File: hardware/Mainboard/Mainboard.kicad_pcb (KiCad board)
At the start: 2 copper layers, 9 parts, among them CN1 NUCLE_F446RE_MORPHO_CN7, CN2 NUCLE_F446RE_MORPHO_CN10, Q2 PSMN5R2-60YL, Q4 PSMN5R2-60YL, Q5 PSMN5R2-60YL, Q6 PSMN5R2-60YL, Q7 AO3400A, Q8 AO3400A, U10 TMC2209_SILENTSTEPSTICK

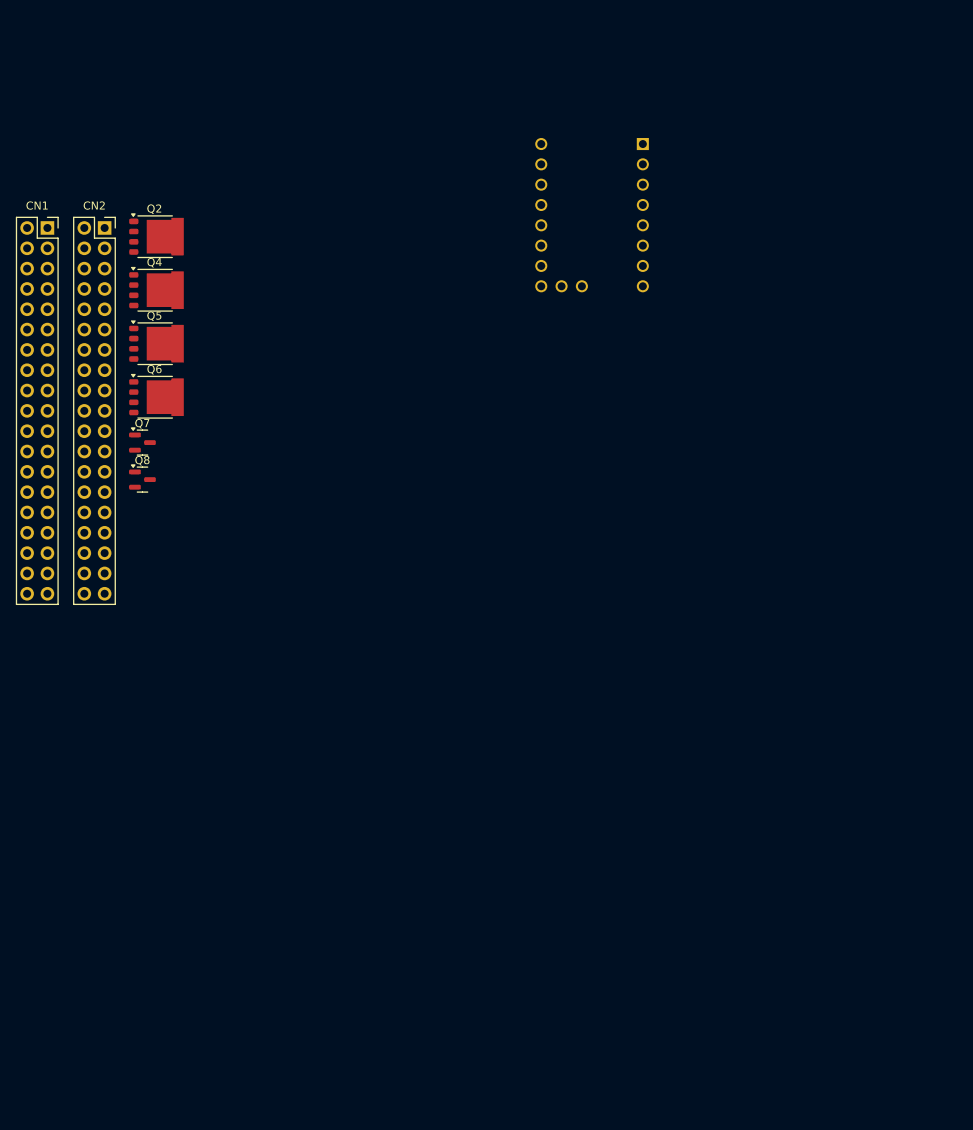
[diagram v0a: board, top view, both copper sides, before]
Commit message: Mainboard-3
Version 3 of Mainboard, (version 2 not uploaded)
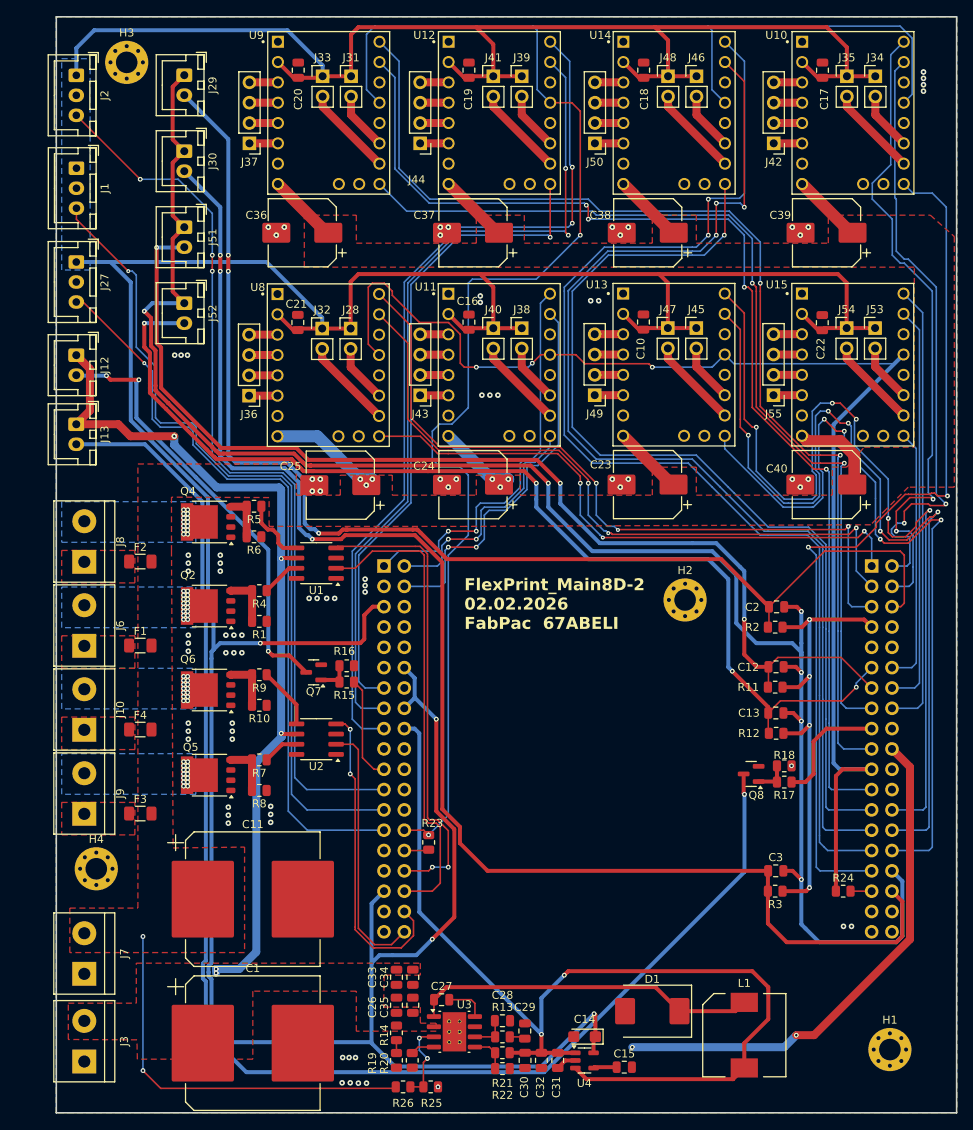
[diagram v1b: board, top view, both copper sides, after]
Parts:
- added C1: 470µ, Capacitor_SMD:CP_Elec_16x17.5, F.Cu at (98.6, 151.0)
- added C10: 100n, Capacitor_SMD:C_0805_2012Metric, F.Cu at (147.4, 60.9)
- added C11: 470µ, Capacitor_SMD:CP_Elec_16x17.5, F.Cu at (98.6, 133.0)
- added C12: 10u, Capacitor_SMD:C_0805_2012Metric, F.Cu at (164.0, 104.0)
- added C13: 10u, Capacitor_SMD:C_0805_2012Metric, F.Cu at (163.9, 109.7)
- added C14: 2.2uF (tantal), Capacitor_Tantalum_SMD:CP_EIA-3216-10_Kemet-I, F.Cu at (140.0, 150.2)
- added C15: 470pF, Capacitor_SMD:C_0805_2012Metric, F.Cu at (145.0, 154.0)
- added C16: 100n, Capacitor_SMD:C_0805_2012Metric, F.Cu at (125.6, 60.9)
- added C17: 100n, Capacitor_SMD:C_0805_2012Metric, F.Cu at (169.8, 29.4)
- added C18: 100n, Capacitor_SMD:C_0805_2012Metric, F.Cu at (147.4, 29.4)
- added C19: 100n, Capacitor_SMD:C_0805_2012Metric, F.Cu at (125.6, 29.4)
- added C2: 10u, Capacitor_SMD:C_0805_2012Metric, F.Cu at (164.0, 96.5)
- added C20: 100n, Capacitor_SMD:C_0805_2012Metric, F.Cu at (104.2, 29.4)
- added C21: 100n, Capacitor_SMD:C_0805_2012Metric, F.Cu at (104.2, 60.9)
- added C22: 100n, Capacitor_SMD:C_0805_2012Metric, F.Cu at (169.7, 60.9)
- added C23: 100µ, Capacitor_SMD:CP_Elec_8x10, F.Cu at (147.9, 81.2)
- added C24: 100µ, Capacitor_SMD:CP_Elec_8x10, F.Cu at (126.1, 81.2)
- added C25: 100µ, Capacitor_SMD:CP_Elec_8x10, F.Cu at (109.5, 81.2)
- added C26: 2.2uF, Capacitor_SMD:C_0805_2012Metric, F.Cu at (116.5, 146.3)
- added C27: 0.1uF, Capacitor_SMD:C_0805_2012Metric, F.Cu at (122.2, 145.6)
- added C28: 4.7pF, Capacitor_SMD:C_0805_2012Metric, F.Cu at (129.8, 148.2)
- added C29: 4.7nF, Capacitor_SMD:C_0805_2012Metric, F.Cu at (132.6, 149.5)
- added C3: 10u, Capacitor_SMD:C_0805_2012Metric, F.Cu at (163.9, 129.5)
- added C30: 47uF, Capacitor_SMD:C_0805_2012Metric, F.Cu at (132.6, 153.1)
- added C31: 47uF, Capacitor_SMD:C_0805_2012Metric, F.Cu at (136.7, 153.2)
- added C32: 47uF, Capacitor_SMD:C_0805_2012Metric, F.Cu at (134.6, 153.2)
- added C33: 2.2uF, Capacitor_SMD:C_0805_2012Metric, F.Cu at (116.5, 142.8)
- added C34: 2.2uF, Capacitor_SMD:C_0805_2012Metric, F.Cu at (118.6, 142.8)
- added C35: 2.2uF, Capacitor_SMD:C_0805_2012Metric, F.Cu at (118.6, 146.3)
- added C36: 100µ, Capacitor_SMD:CP_Elec_8x10, F.Cu at (104.8, 49.7)
- added C37: 100µ, Capacitor_SMD:CP_Elec_8x10, F.Cu at (126.1, 49.7)
- added C38: 100µ, Capacitor_SMD:CP_Elec_8x10, F.Cu at (147.9, 49.7)
- added C39: 100µ, Capacitor_SMD:CP_Elec_8x10, F.Cu at (170.3, 49.7)
- added C40: 100µ, Capacitor_SMD:CP_Elec_8x10, F.Cu at (170.3, 81.2)
- added D1: B560C, Diode_SMD:D_SMC, F.Cu at (148.5, 147.0)
- added F1: 3A, Fuse:Fuse_1206_3216Metric, F.Cu at (84.5, 101.3)
- added F2: 3A, Fuse:Fuse_1206_3216Metric, F.Cu at (84.5, 90.8)
- added F3: 15A, Fuse:Fuse_1206_3216Metric, F.Cu at (84.5, 122.3)
- added F4: Fuse, Fuse:Fuse_1206_3216Metric, F.Cu at (84.5, 111.8)
- added H1: MountingHole, MountingHole:MountingHole_2.7mm_M2.5_Pad_Via, F.Cu at (178.2, 151.8)
- added H2: MountingHole, MountingHole:MountingHole_2.7mm_M2.5_Pad_Via, F.Cu at (152.6, 95.6)
- added H3: MountingHole, MountingHole:MountingHole_2.7mm_M2.5_Pad_Via, F.Cu at (82.8, 28.4)
- added H4: MountingHole, MountingHole:MountingHole_2.7mm_M2.5_Pad_Via, F.Cu at (79.0, 129.2)
- added J1: X_END, Connector_JST:JST_XH_B3B-XH-A_1x03_P2.50mm_Vertical, F.Cu at (76.5, 41.6)
- added J10: Power, TerminalBlock:TerminalBlock_bornier-2_P5.08mm, F.Cu at (77.5, 111.8)
- added J12: Part_Cooling2, Connector_JST:JST_XH_B2B-XH-A_1x02_P2.50mm_Vertical, F.Cu at (76.5, 65.0)
- added J13: Part_Cooling1, Connector_JST:JST_XH_B2B-XH-A_1x02_P2.50mm_Vertical, F.Cu at (76.5, 73.6)
- added J2: Y_END, Connector_JST:JST_XH_B3B-XH-A_1x03_P2.50mm_Vertical, F.Cu at (76.5, 30.0)
- added J27: Z_END, Connector_JST:JST_XH_B3B-XH-A_1x03_P2.50mm_Vertical, F.Cu at (76.5, 53.4)
- added J28: X_MS2, Connector_PinHeader_2.54mm:PinHeader_1x02_P2.54mm_Vertical, F.Cu at (110.8, 61.7)
- added J29: HE1_therm, Connector_JST:JST_XH_B2B-XH-A_1x02_P2.50mm_Vertical, F.Cu at (90.0, 30.0)
- added J3: +12V, TerminalBlock:TerminalBlock_bornier-2_P5.08mm, F.Cu at (77.5, 153.3)
- added J30: Bed_therm, Connector_JST:JST_XH_B2B-XH-A_1x02_P2.50mm_Vertical, F.Cu at (90.0, 39.5)
- added J31: Z1_MS2, Connector_PinHeader_2.54mm:PinHeader_1x02_P2.54mm_Vertical, F.Cu at (110.8, 30.1)
- added J32: X_MS1, Connector_PinHeader_2.54mm:PinHeader_1x02_P2.54mm_Vertical, F.Cu at (107.2, 61.7)
- added J33: Z1_MS1, Connector_PinHeader_2.54mm:PinHeader_1x02_P2.54mm_Vertical, F.Cu at (107.3, 30.1)
- added J34: Z4_MS2, Connector_PinHeader_2.54mm:PinHeader_1x02_P2.54mm_Vertical, F.Cu at (176.4, 30.1)
- added J35: Z4_MS1, Connector_PinHeader_2.54mm:PinHeader_1x02_P2.54mm_Vertical, F.Cu at (172.8, 30.1)
- added J36: X_Motor, Connector_PinHeader_2.54mm:PinHeader_1x04_P2.54mm_Vertical, F.Cu at (98.1, 70.1)
- added J37: Z1_Motor, Connector_PinHeader_2.54mm:PinHeader_1x04_P2.54mm_Vertical, F.Cu at (98.1, 38.5)
- added J38: Y_MS2, Connector_PinHeader_2.54mm:PinHeader_1x02_P2.54mm_Vertical, F.Cu at (132.2, 61.6)
- added J39: Z2_MS2, Connector_PinHeader_2.54mm:PinHeader_1x02_P2.54mm_Vertical, F.Cu at (132.2, 30.1)
- added J40: Y_MS1, Connector_PinHeader_2.54mm:PinHeader_1x02_P2.54mm_Vertical, F.Cu at (128.6, 61.6)
- added J41: Z2_MS1, Connector_PinHeader_2.54mm:PinHeader_1x02_P2.54mm_Vertical, F.Cu at (128.6, 30.1)
- added J42: Z4_Motor, Connector_PinHeader_2.54mm:PinHeader_1x04_P2.54mm_Vertical, F.Cu at (163.7, 38.5)
- added J43: Y_Motor, Connector_PinHeader_2.54mm:PinHeader_1x04_P2.54mm_Vertical, F.Cu at (119.5, 70.0)
- added J44: Z2_Motor, Connector_PinHeader_2.54mm:PinHeader_1x04_P2.54mm_Vertical, F.Cu at (119.5, 38.5)
- added J45: E_MS2, Connector_PinHeader_2.54mm:PinHeader_1x02_P2.54mm_Vertical, F.Cu at (154.0, 61.6)
- added J46: Z3_MS2, Connector_PinHeader_2.54mm:PinHeader_1x02_P2.54mm_Vertical, F.Cu at (154.0, 30.1)
- added J47: E_MS1, Connector_PinHeader_2.54mm:PinHeader_1x02_P2.54mm_Vertical, F.Cu at (150.4, 61.6)
- added J48: Z3_MS1, Connector_PinHeader_2.54mm:PinHeader_1x02_P2.54mm_Vertical, F.Cu at (150.5, 30.1)
- added J49: E_Motor, Connector_PinHeader_2.54mm:PinHeader_1x04_P2.54mm_Vertical, F.Cu at (141.3, 70.0)
- added J50: Z3_Motor, Connector_PinHeader_2.54mm:PinHeader_1x04_P2.54mm_Vertical, F.Cu at (141.3, 38.5)
- added J51: PWR_therm, Connector_JST:JST_XH_B2B-XH-A_1x02_P2.50mm_Vertical, F.Cu at (90.0, 49.0)
- added J52: HE2_therm, Connector_JST:JST_XH_B2B-XH-A_1x02_P2.50mm_Vertical, F.Cu at (90.0, 58.5)
- added J53: R_MS2, Connector_PinHeader_2.54mm:PinHeader_1x02_P2.54mm_Vertical, F.Cu at (176.4, 61.6)
- added J54: R_MS1, Connector_PinHeader_2.54mm:PinHeader_1x02_P2.54mm_Vertical, F.Cu at (172.8, 61.6)
- added J55: R_Motor, Connector_PinHeader_2.54mm:PinHeader_1x04_P2.54mm_Vertical, F.Cu at (163.7, 70.0)
- added J6: Hotend1, TerminalBlock:TerminalBlock_bornier-2_P5.08mm, F.Cu at (77.5, 101.3)
- added J7: +24V, TerminalBlock:TerminalBlock_bornier-2_P5.08mm, F.Cu at (77.5, 142.3)
- added J8: Hotend2, TerminalBlock:TerminalBlock_bornier-2_P5.08mm, F.Cu at (77.5, 90.8)
- added J9: Bed, TerminalBlock:TerminalBlock_bornier-2_P5.08mm, F.Cu at (77.5, 122.3)
- added L1: 7.2uH, Inductor_SMD:L_Wuerth_WE-PDF, F.Cu at (160.0, 150.0)
- added R1: 100k, Resistor_SMD:R_0805_2012Metric, F.Cu at (99.4, 98.3)
- added R10: 100k, Resistor_SMD:R_0805_2012Metric, F.Cu at (99.4, 108.8)
- added R11: 4k7, Resistor_SMD:R_0805_2012Metric, F.Cu at (163.9, 106.5)
- added R12: 4k7, Resistor_SMD:R_0805_2012Metric, F.Cu at (164.0, 112.3)
- added R13: 16.9k, Resistor_SMD:R_0805_2012Metric, F.Cu at (129.8, 150.2)
- added R14: 442k, Resistor_SMD:R_0805_2012Metric, F.Cu at (116.5, 149.7)
- added R15: 100R, Resistor_SMD:R_0805_2012Metric, F.Cu at (110.3, 105.9)
- added R16: 100k, Resistor_SMD:R_0805_2012Metric, F.Cu at (110.3, 103.8)
- added R17: 100R, Resistor_SMD:R_0805_2012Metric, F.Cu at (165.0, 118.4)
- added R18: 100k, Resistor_SMD:R_0805_2012Metric, F.Cu at (165.0, 116.3)
- added R19: 90.9k, Resistor_SMD:R_0805_2012Metric, F.Cu at (116.5, 153.1)
- added R2: 4k7, Resistor_SMD:R_0805_2012Metric, F.Cu at (163.9, 99.0)
- added R20: 243k, Resistor_SMD:R_0805_2012Metric, F.Cu at (118.5, 153.1)
- added R21: 53.6k, Resistor_SMD:R_0805_2012Metric, F.Cu at (129.8, 152.2)
- added R22: 10.2k, Resistor_SMD:R_0805_2012Metric, F.Cu at (129.8, 154.2)
- added R23: 1k, Resistor_SMD:R_0805_2012Metric, F.Cu at (120.5, 125.9)
- added R24: 1k, Resistor_SMD:R_0805_2012Metric, F.Cu at (172.4, 132.0)
- added R25: 11k, Resistor_SMD:R_0805_2012Metric, F.Cu at (120.8, 156.5)
- added R26: 100k, Resistor_SMD:R_0805_2012Metric, F.Cu at (117.3, 156.5)
- added R3: 4k7, Resistor_SMD:R_0805_2012Metric, F.Cu at (163.9, 132.0)
- added R4: 50R, Resistor_SMD:R_0805_2012Metric, F.Cu at (99.4, 94.4)
- added R5: 50R, Resistor_SMD:R_0805_2012Metric, F.Cu at (98.7, 83.9)
- added R6: 100k, Resistor_SMD:R_0805_2012Metric, F.Cu at (98.7, 87.7)
- added R7: 50R, Resistor_SMD:R_0805_2012Metric, F.Cu at (99.4, 115.6)
- added R8: 100k, Resistor_SMD:R_0805_2012Metric, F.Cu at (99.4, 119.4)
- added R9: 50R, Resistor_SMD:R_0805_2012Metric, F.Cu at (99.4, 104.9)
- added U1: MIC4426, Package_SO:SOIC-8_3.9x4.9mm_P1.27mm, F.Cu at (106.5, 91.0)
- added U11: Y, FlexPrint:MODULE_TMC2209_SILENTSTEPSTICK, F.Cu at (129.4, 66.2)
- added U12: Z2, FlexPrint:MODULE_TMC2209_SILENTSTEPSTICK, F.Cu at (129.4, 34.7)
- added U13: E, FlexPrint:MODULE_TMC2209_SILENTSTEPSTICK, F.Cu at (151.2, 66.2)
- added U14: Z3, FlexPrint:MODULE_TMC2209_SILENTSTEPSTICK, F.Cu at (151.2, 34.7)
- added U15: R, FlexPrint:MODULE_TMC2209_SILENTSTEPSTICK, F.Cu at (173.6, 66.2)
- added U2: MIC4426, Package_SO:SOIC-8_3.9x4.9mm_P1.27mm, F.Cu at (106.5, 113.0)
- added U3: TPS54560BDDA, Package_SO:Texas_R-PDSO-G8_EP2.95x4.9mm_Mask2.4x3.1mm_ThermalVias, F.Cu at (123.8, 149.6)
- added U4: MIC5219-3.3YM5, Package_TO_SOT_SMD:SOT-23-5, F.Cu at (140.0, 153.2)
- added U8: X, FlexPrint:MODULE_TMC2209_SILENTSTEPSTICK, F.Cu at (108.0, 66.2)
- added U9: Z1, FlexPrint:MODULE_TMC2209_SILENTSTEPSTICK, F.Cu at (108.1, 34.7)
- CN1, CN2: moved to B.Cu
- U10: value TMC2209_SILENTSTEPSTICK -> Z4; moved to F.Cu
- moved CN2 104.8 mm to (175.9, 91.4), turned to 180 degrees
- moved Q8 84.5 mm to (160.9, 117.3), turned to 180 degrees
- moved CN1 59.6 mm to (115.0, 91.4), turned to 180 degrees
- moved Q5 54.4 mm to (93.1, 117.5), turned to 180 degrees
- moved Q2 46.7 mm to (93.1, 96.4), turned to 180 degrees
- moved Q6 37.2 mm to (93.1, 106.9), turned to 180 degrees
- moved Q7 35.8 mm to (106.2, 104.6), turned to 180 degrees
- moved U10 35.0 mm to (173.6, 34.7), turned to 0 degrees
- moved Q4 29.8 mm to (93.1, 85.8), turned to 180 degrees
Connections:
- CN1 pad 1: unconnected-(CN1-Pin_1-Pad1) -> Y_DIR
- CN1 pad 13: unconnected-(CN1-Pin_13-Pad13) -> Z2_EN
- CN1 pad 15: unconnected-(CN1-Pin_15-Pad15) -> Z2_STEP
- CN1 pad 17: unconnected-(CN1-Pin_17-Pad17) -> Z2_DIR
- CN1 pad 2: unconnected-(CN1-Pin_2-Pad2) -> Y_EN
- CN1 pad 21: unconnected-(CN1-Pin_21-Pad21) -> PCF2
- CN1 pad 23: X_END -> Y_END
- CN1 pad 25: Y_END -> X_END
- CN1 pad 28: PCF2 -> uart2_tmc
- CN1 pad 30: PCF1 -> Net-(CN1-Pin_30)
- CN1 pad 4: unconnected-(CN1-Pin_4-Pad4) -> Y_STEP
- CN2 pad 12: Y_EN -> R_EN
- CN2 pad 14: Y_STEP -> R_STEP
- CN2 pad 16: Y_DIR -> R_DIR
- CN2 pad 17: Z1_STEP -> PCF1
- CN2 pad 2: unconnected-(CN2-Pin_2-Pad2) -> Z4_STEP
- CN2 pad 21: Z2_EN -> uart1_tmc
- CN2 pad 23: Z2_STEP -> Z1_STEP
- CN2 pad 25: Z2_DIR -> Z3_EN
- CN2 pad 27: Z3_EN -> Z3_STEP
- CN2 pad 29: Z3_STEP -> Z3_DIR
- CN2 pad 31: Z3_DIR -> Z4_EN
- CN2 pad 33: Z4_EN -> Net-(CN2-Pin_33)
- CN2 pad 35: Z4_STEP -> unconnected-(CN2-Pin_35-Pad35)
- CN2 pad 37: Z4_DIR -> unconnected-(CN2-Pin_37-Pad37)
- CN2 pad 4: unconnected-(CN2-Pin_4-Pad4) -> Z4_DIR
- U10 pad 12: /M_UART -> uart2_tmc
- U10 pad 18: /M_DIAG -> unconnected-(U10-DIAG-Pad18)
- U10 pad 2: Net-(U10-VIO) -> +3V3
- U10 pad 3: /Z4_1B -> /Z4_1A
- U10 pad 4: /Z4_1A -> /Z4_2A
- U10 pad 5: /Z4_2A -> /Z4_1B
- U10 pad 8: Net-(U10-VM) -> +24V
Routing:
- net +3V3: track 0.00 -> 581.2 mm, vias 0 -> 4
- net uart2_tmc: track 0.00 -> 224.5 mm, vias 0 -> 2
- net GNDA: track 0.00 -> 219.9 mm, vias 0 -> 6
- net Bed_therm: track 0.00 -> 181.3 mm, vias 0 -> 3
- net Net-(J13-Pin_2): track 0.00 -> 177.5 mm, vias 0 -> 1
- net uart1_tmc: track 0.00 -> 164.8 mm, vias 0 -> 3
- net HE1_therm: track 0.00 -> 156.6 mm, vias 0 -> 3
- net Z3_DIR: track 0.00 -> 150.0 mm, vias 0 -> 2
- net Z3_STEP: track 0.00 -> 145.0 mm, vias 0 -> 3
- net Z1_STEP: track 0.00 -> 142.2 mm, vias 0 -> 4
- net Z1_DIR: track 0.00 -> 139.5 mm, vias 0 -> 2
- net +24V: track 0.00 -> 137.9 mm, vias 0 -> 8
- net PWR_therm: track 0.00 -> 136.9 mm, vias 0 -> 3
- net HE2_therm: track 0.00 -> 134.7 mm, vias 0 -> 4
- net +5V: track 0.00 -> 125.3 mm, vias 0 -> 2
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- added copper zone on F.Cu, net +12V
- added copper zone on F.Cu, net +24V
- added copper zone on B.Cu, net +3V3
- added copper zone on B.Cu, net GND
- added copper zone on F.Cu, net GND
- added copper zone on F.Cu, net Net-(J10-Pin_1)
- added copper zone on B.Cu, net Net-(J10-Pin_2)
- added copper zone on F.Cu, net Net-(J6-Pin_1)
- added copper zone on B.Cu, net Net-(J6-Pin_2)
- added copper zone on F.Cu, net Net-(J8-Pin_1)
- added copper zone on B.Cu, net Net-(J8-Pin_2)
- added copper zone on F.Cu, net Net-(J9-Pin_1)
- added copper zone on B.Cu, net Net-(J9-Pin_2)
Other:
- board outline added: 112.5 x 137 mm
- board text added: "FlexPrint_Main8D-2 02.02.2026 FabPac 67ABELI"

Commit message: mainboard v2
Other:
- board text added: "FlexPrint-Main8D-3 2026-02-06 FabPac 67ABELI"
- board text removed: "FlexPrint_Main8D-2 02.02.2026 FabPac 67ABELI"
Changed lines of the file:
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@@
 		)
 		(embedded_fonts no)
-		(model "${KICAD9_3DMODEL_DIR}/Package_SO.3dshapes/Texas_R-PDSO-G8_EP2.95x4.9mm_Mask2.4x3.1mm.wrl"
+		(model "${KICAD9_3DMODEL_DIR}/Package_SO.3dshapes/Texas_HTSOP-8-1EP_3.9x4.9mm_P1.27mm_EP2.85x4.9mm_Mask2.4x3.1mm_ThermalVias.wrl"
 			(offset
 				(xyz 0 0 0)
@@
 		(tags "Choke Shielded Power Inductor WE-PDF Wuerth")
 		(property "Reference" "L1"
-			(at -6.5 0 180)
+			(at -6.5 0 0)
 			(layer "F.SilkS")
 			(effects
@@
 		)
 		(embedded_fonts no)
-		(model "${KICAD9_3DMODEL_DIR}/Inductor_SMD.3dshapes/L_Wuerth_WE-PDF.wrl"
+		(model "${DOWNLOADS}/ul_7447798720/Download_STP_WE-PDF-1064_rev1.stp"
 			(offset
 				(xyz 0 0 0)
@@
 		(model "${KICAD9_3DMODEL_DIR}/Connector_PinSocket_2.54mm.3dshapes/PinSocket_2x19_P2.54mm_Vertical.wrl"
 			(offset
-				(xyz 0 0 0)
+				(xyz -2.5 0 -1.5)
 			)
 			(scale
@@
 			)
 			(rotate
-				(xyz 0 0 0)
+				(xyz -0 -180 -0)
 			)
 		)
@@
 		(model "${KICAD9_3DMODEL_DIR}/Connector_PinSocket_2.54mm.3dshapes/PinSocket_2x19_P2.54mm_Vertical.wrl"
 			(offset
-				(xyz 0 0 0)
+				(xyz -2.5 0 -1.5)
 			)
 			(scale
@@
 			)
 			(rotate
-				(xyz 0 0 0)
+				(xyz -0 -180 -0)
 			)
 		)
@@
 		(layer "Edge.Cuts")
 	)
-	(gr_text "FlexPrint_Main8D-2\n02.02.2026\nFabPac  67ABELI"
+	(gr_text "FlexPrint-Main8D-3\n2026-02-06\nFabPac  67ABELI"
 		(at 125 99.4 0)
 		(layer "F.SilkS")
@@
 		)
 	)
-	(group ""
-		(members "048fcc33-521f-405f-a3b4-84bea92967a4" "26936854-e54c-4f50-8b33-9aa561615916"
-			"3c914597-01ca-46de-885b-16f9a62684c9" "9b9f7521-c1e4-4015-8d2c-53375a615cd6"
-		)
-	)
